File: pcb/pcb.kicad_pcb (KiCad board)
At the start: 2 copper layers, 50 x 60 mm, 66 parts, among them J1 Battery, J10 Conn_01x04_Male, J11 STM32_SWD, J2 MOTOR_Vcc, J3 MOTOR_5V, J4 MOTOR_OUT, J5 US_SENSOR, J6 BUMPER_SENSOR_FRONT, J7 BUMPER_SENSOR_BACK, J8 BT_USART, J9 GPIO, SW1 SW_Push, U1 LM317_TO-252, U2 L293D, U3 AMS1117-5.0, U4 AMS1117-3.3, U5 STM32F103C8T6, Y1 X322516MLB4SI

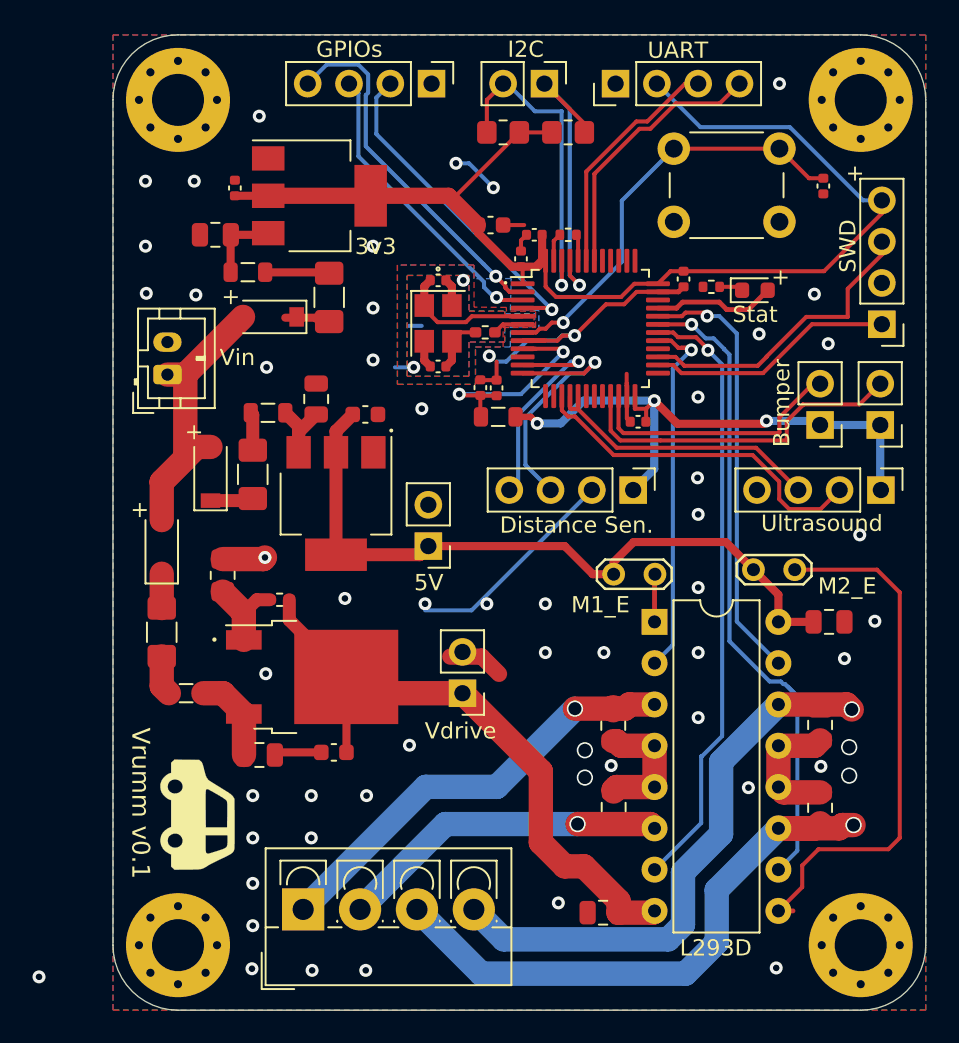
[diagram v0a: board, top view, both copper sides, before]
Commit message: SWD fix on pcb
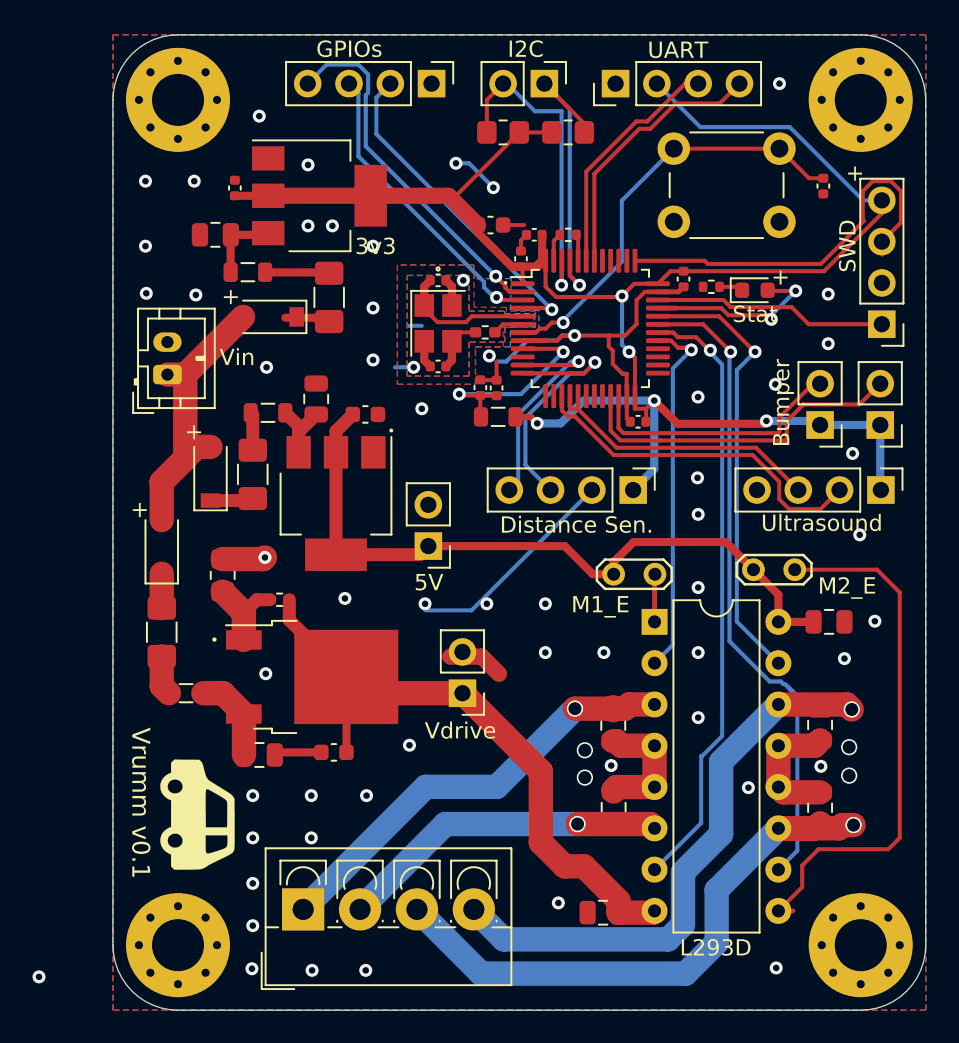
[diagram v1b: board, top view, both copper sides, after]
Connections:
- U5 pad 26: SYS_SWDIO -> Net-(U5-Pad26)
- U5 pad 27: SYS_SWCLK -> Net-(U5-Pad27)
- U5 pad 34: Net-(U5-Pad34) -> SYS_SWDIO
- U5 pad 37: Net-(U5-Pad37) -> SYS_SWCLK
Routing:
- net +3V3: track 114.5 -> 121.0 mm, vias 3 -> 5
- net SYS_SWCLK: track 18.7 -> 24.4 mm
- net GND: track 74.1 -> 77.9 mm, vias 58 -> 62
- net Net-(D4-Pad2): track 7.59 -> 11.4 mm, vias 0 -> 2
- net SYS_SWDIO: track 15.2 -> 14.4 mm
- net MOTOR2_CH2: track 26.8 -> 27.6 mm

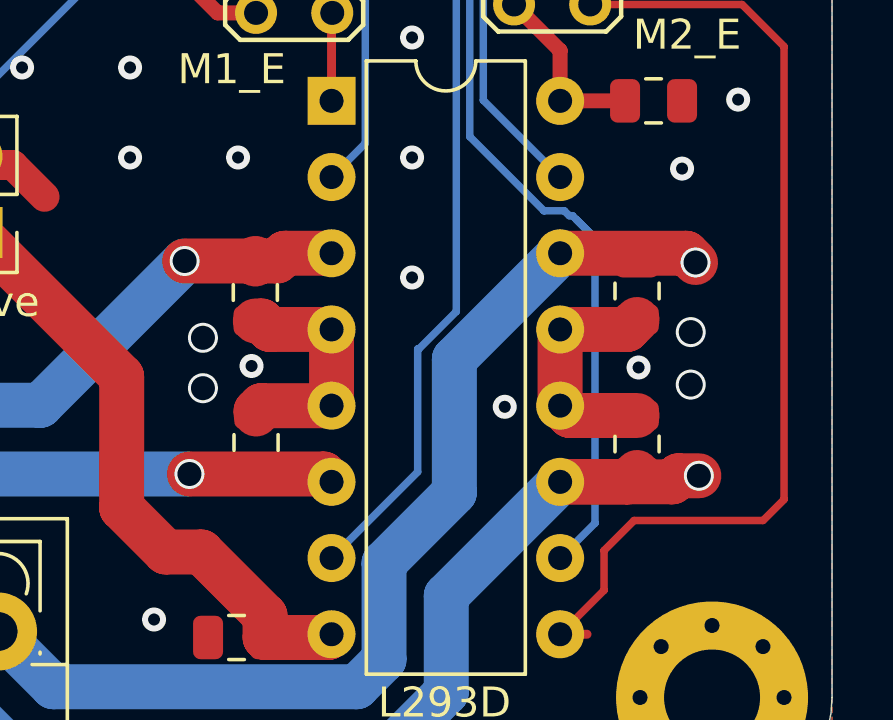
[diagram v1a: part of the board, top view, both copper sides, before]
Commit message: PCB: voltage divider on motor power
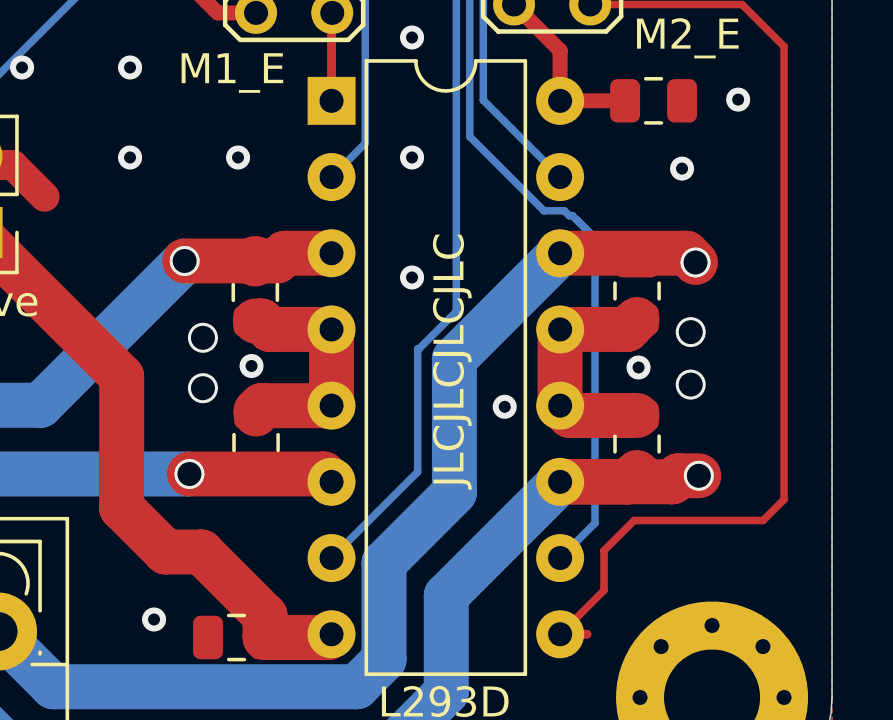
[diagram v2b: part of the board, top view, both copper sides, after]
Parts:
- R1: value 5.6k -> 1.5k
- R2: value 1k -> 240
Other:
- board text added: "+9.1V"
- board text added: "JLCJLCJLCJLC"
- board text added: "VCC"
- board text removed: "+8.5V"
- board text removed: "Vcc"
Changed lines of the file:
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@@
   (general
     (thickness 1.6)
-    (drawings 65)
+    (drawings 66)
     (tracks 531)
     (zones 0)
@@
       (effects (font (size 1 1) (thickness 0.15)))
     )
-    (fp_text value 1k (at 0 1.17) (layer F.Fab)
+    (fp_text value 240 (at 0 1.17) (layer F.Fab)
       (effects (font (size 1 1) (thickness 0.15)))
     )
@@
       (effects (font (size 1 1) (thickness 0.15)))
     )
-    (fp_text value 5.6k (at 0 1.65 90) (layer F.Fab)
+    (fp_text value 1.5k (at 0 1.65 90) (layer F.Fab)
       (effects (font (size 1 1) (thickness 0.15)))
     )
@@
     )
   )
+  (gr_text JLCJLCJLCJLC (at 49.25 56.75 90) (layer F.SilkS)
+    (effects (font (size 1 1) (thickness 0.15)))
+  )
   (gr_text + (at 57.65 20.5) (layer F.SilkS)
     (effects (font (size 1 1) (thickness 0.15)))
@@
     (effects (font (size 1 1) (thickness 0.15)) (justify mirror))
   )
-  (gr_text +8.5V (at 29.84 52.41) (layer B.SilkS)
+  (gr_text +9.1V (at 29.84 52.41) (layer B.SilkS)
     (effects (font (size 1 1) (thickness 0.15)) (justify mirror))
   )
@@
     (effects (font (size 1 1) (thickness 0.15)) (justify mirror))
   )
-  (gr_text Vcc (at 18.3 32.8) (layer B.SilkS)
+  (gr_text VCC (at 18.5 34) (layer B.SilkS)
     (effects (font (size 1 1) (thickness 0.15)) (justify mirror))
   )

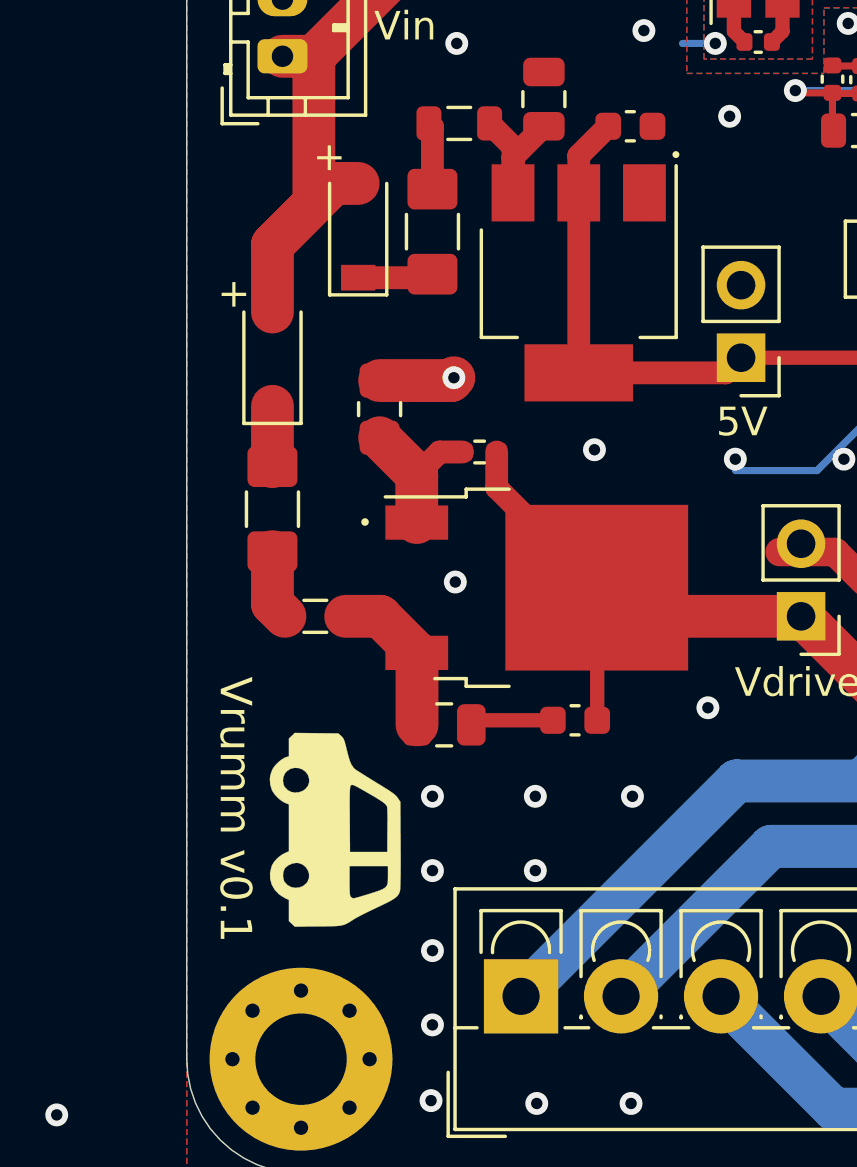
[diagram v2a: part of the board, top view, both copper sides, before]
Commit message: pcb versioning on silk layer, 5v track width
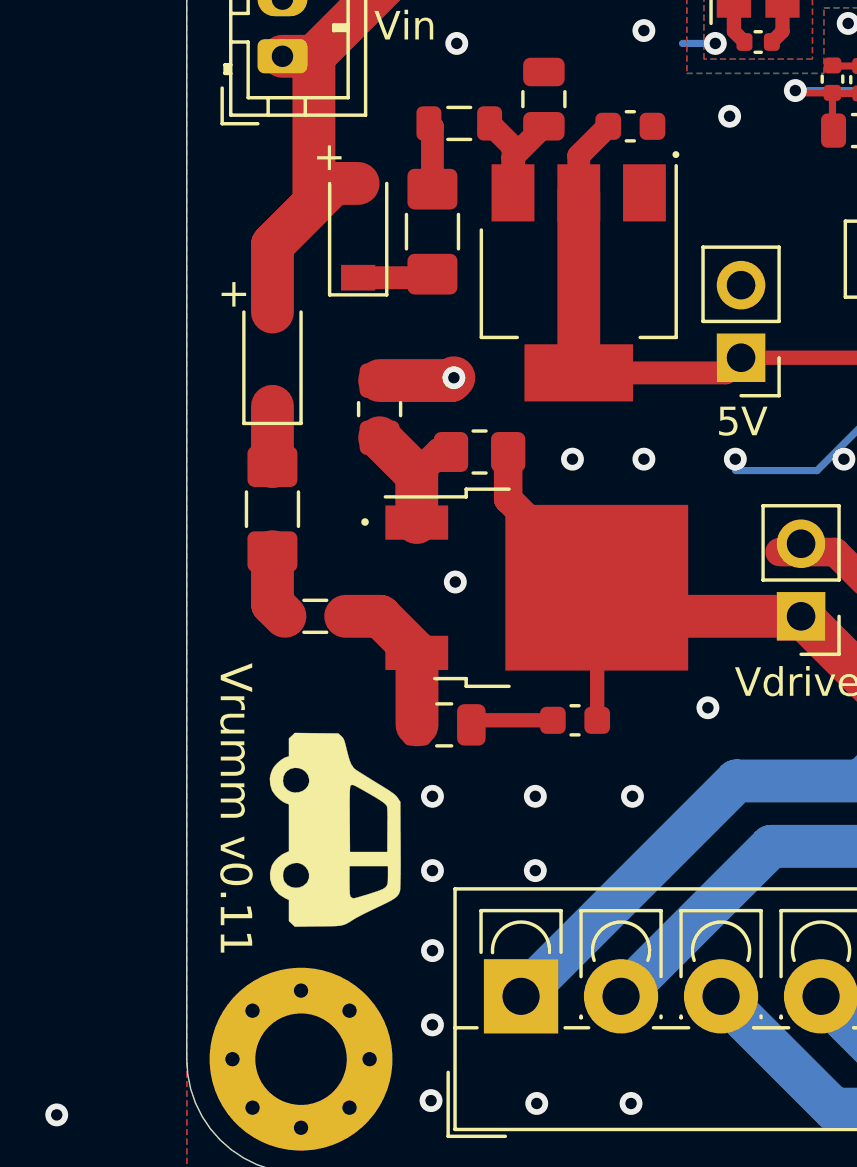
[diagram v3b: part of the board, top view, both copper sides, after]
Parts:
- R2: footprint Resistor_SMD:R_0402_1005Metric_Pad0.72x0.64mm_HandSolder -> Resistor_SMD:R_0805_2012Metric_Pad1.20x1.40mm_HandSolder
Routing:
- net GND: vias 62 -> 63
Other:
- board text added: "Vrumm v0.11"
- board text removed: "Vrumm v0.1"
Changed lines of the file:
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@@
     (thickness 1.6)
     (drawings 66)
-    (tracks 531)
+    (tracks 532)
     (zones 0)
     (modules 66)
@@
   )
   (setup
-    (last_trace_width 0.25)
+    (last_trace_width 1.5)
     (user_trace_width 0.3)
     (user_trace_width 0.4)
@@
     (add_net WHEEL_SENSOR_R)
   )
+  (module Resistor_SMD:R_0805_2012Metric_Pad1.20x1.40mm_HandSolder (layer F.Cu)
+    (at 22.25 46.75 180)
+    (descr "Resistor SMD 0805 (2012 Metric), square (rectangular) end terminal, IPC_7351 nominal with elongated pad for handsoldering. (Body size source: IPC-SM-782 page 72, https://www.pcb-3d.com/wordpress/wp-content/uploads/ipc-sm-782a_amendment_1_and_2.pdf), generated with kicad-footprint-generator")
+    (tags "resistor handsolder")
+    (attr smd)
+    (fp_text reference R2 (at 0 -1.65) (layer F.Fab)
+      (effects (font (size 1 1) (thickness 0.15)))
+    )
+    (fp_text value 240 (at 0 1.65) (layer F.Fab)
+      (effects (font (size 1 1) (thickness 0.15)))
+    )
+    (fp_text user %R (at 0 0) (layer F.Fab)
+      (effects (font (size 0.5 0.5) (thickness 0.08)))
+    )
+    (fp_line (start -1 0.625) (end -1 -0.625) (layer F.Fab) (width 0.1))
+    (fp_line (start -1 -0.625) (end 1 -0.625) (layer F.Fab) (width 0.1))
+    (fp_line (start 1 -0.625) (end 1 0.625) (layer F.Fab) (width 0.1))
+    (fp_line (start 1 0.625) (end -1 0.625) (layer F.Fab) (width 0.1))
+    (fp_line (start -0.227064 -0.735) (end 0.227064 -0.735) (layer F.SilkS) (width 0.12))
+    (fp_line (start -0.227064 0.735) (end 0.227064 0.735) (layer F.SilkS) (width 0.12))
+    (fp_line (start -1.85 0.95) (end -1.85 -0.95) (layer F.CrtYd) (width 0.05))
+    (fp_line (start -1.85 -0.95) (end 1.85 -0.95) (layer F.CrtYd) (width 0.05))
+    (fp_line (start 1.85 -0.95) (end 1.85 0.95) (layer F.CrtYd) (width 0.05))
+    (fp_line (start 1.85 0.95) (end -1.85 0.95) (layer F.CrtYd) (width 0.05))
+    (pad 2 smd roundrect (at 1 0 180) (size 1.2 1.4) (layers F.Cu F.Paste F.Mask) (roundrect_rratio 0.2083325)
+      (net 60 "Net-(R1-Pad2)"))
+    (pad 1 smd roundrect (at -1 0 180) (size 1.2 1.4) (layers F.Cu F.Paste F.Mask) (roundrect_rratio 0.2083325)
+      (net 44 Vdrive))
+    (model ${KISYS3DMOD}/Resistor_SMD.3dshapes/R_0805_2012Metric.wrl
+      (at (xyz 0 0 0))
+      (scale (xyz 1 1 1))
+      (rotate (xyz 0 0 0))
+    )
+  )
   (module Crystal:Crystal_SMD_3225-4Pin_3.2x2.5mm (layer F.Cu)
     (at 32 29.75 270)
@@
   (module logo_car:logo_car (layer F.Cu)
     (at 17.28 60 270)
+    (attr smd)
     (fp_text reference G*** (at 0 0 90) (layer F.SilkS) hide
       (effects (font (size 1.524 1.524) (thickness 0.3)))
@@
     )
   )
-  (module Resistor_SMD:R_0402_1005Metric_Pad0.72x0.64mm_HandSolder (layer F.Cu)
-    (at 22.25 46.75 180)
-    (descr "Resistor SMD 0402 (1005 Metric), square (rectangular) end terminal, IPC_7351 nominal with elongated pad for handsoldering. (Body size source: IPC-SM-782 page 72, https://www.pcb-3d.com/wordpress/wp-content/uploads/ipc-sm-782a_amendment_1_and_2.pdf), generated with kicad-footprint-generator")
-    (tags "resistor handsolder")
-    (attr smd)
-    (fp_text reference R2 (at -58.5 -4) (layer F.Fab)
-      (effects (font (size 1 1) (thickness 0.15)))
-    )
-    (fp_text value 240 (at 0 1.17) (layer F.Fab)
-      (effects (font (size 1 1) (thickness 0.15)))
-    )
-    (fp_line (start 1.1 0.47) (end -1.1 0.47) (layer F.CrtYd) (width 0.05))
-    (fp_line (start 1.1 -0.47) (end 1.1 0.47) (layer F.CrtYd) (width 0.05))
-    (fp_line (start -1.1 -0.47) (end 1.1 -0.47) (layer F.CrtYd) (width 0.05))
-    (fp_line (start -1.1 0.47) (end -1.1 -0.47) (layer F.CrtYd) (width 0.05))
-    (fp_line (start -0.167621 0.38) (end 0.167621 0.38) (layer F.SilkS) (width 0.12))
-    (fp_line (start -0.167621 -0.38) (end 0.167621 -0.38) (layer F.SilkS) (width 0.12))
-    (fp_line (start 0.525 0.27) (end -0.525 0.27) (layer F.Fab) (width 0.1))
-    (fp_line (start 0.525 -0.27) (end 0.525 0.27) (layer F.Fab) (width 0.1))
-    (fp_line (start -0.525 -0.27) (end 0.525 -0.27) (layer F.Fab) (width 0.1))
-    (fp_line (start -0.525 0.27) (end -0.525 -0.27) (layer F.Fab) (width 0.1))
-    (fp_text user %R (at 0 0) (layer F.Fab)
-      (effects (font (size 0.26 0.26) (thickness 0.04)))
-    )
-    (pad 2 smd roundrect (at 0.5975 0 180) (size 0.715 0.64) (layers F.Cu F.Paste F.Mask) (roundrect_rratio 0.25)
-      (net 60 "Net-(R1-Pad2)"))
-    (pad 1 smd roundrect (at -0.5975 0 180) (size 0.715 0.64) (layers F.Cu F.Paste F.Mask) (roundrect_rratio 0.25)
-      (net 44 Vdrive))
-    (model ${KISYS3DMOD}/Resistor_SMD.3dshapes/R_0402_1005Metric.wrl
-      (at (xyz 0 0 0))
-      (scale (xyz 1 1 1))
-      (rotate (xyz 0 0 0))
-    )
-  )
   (module Resistor_SMD:R_0805_2012Metric_Pad1.20x1.40mm_HandSolder (layer F.Cu)
     (at 18.75 45.25 270)
@@
     (effects (font (size 0.8 0.8) (thickness 0.15)) (justify mirror))
   )
-  (gr_text "Vrumm v0.1" (at 13.7 59.27 270) (layer F.SilkS)
+  (gr_text "Vrumm v0.11" (at 13.7 59.27 270) (layer F.SilkS)
     (effects (font (size 1.1 1.1) (thickness 0.2)))
   )
@@
   (segment (start 16.45 38.05) (end 15 39.5) (width 1.5) (layer F.Cu) (net 1))
   (segment (start 16.45 32.9) (end 16.45 38.05) (width 1.5) (layer F.Cu) (net 1))
-  (via (at 26.27 46.67) (size 0.8) (drill 0.4) (layers F.Cu B.Cu) (net 2))
+  (via (at 25.5 47) (size 0.8) (drill 0.4) (layers F.Cu B.Cu) (net 2))
   (via (at 40.4 30.5) (size 0.8) (drill 0.4) (layers F.Cu B.Cu) (net 2))
   (via (at 30.5 32.45) (size 0.8) (drill 0.4) (layers F.Cu B.Cu) (net 2))
@@
   (via (at 25.5 23.75) (size 0.8) (drill 0.4) (layers F.Cu B.Cu) (net 2))
   (via (at 24 20) (size 0.8) (drill 0.4) (layers F.Cu B.Cu) (net 2))
+  (via (at 28 47) (size 0.8) (drill 0.4) (layers F.Cu B.Cu) (net 2))
   (via (at 43.75 31.5) (size 0.8) (drill 0.4) (layers F.Cu B.Cu) (net 11))
   (via (at 52.5 29.5) (size 0.8) (drill 0.4) (layers F.Cu B.Cu) (net 18))
   (segment (start 25.72 36.38) (end 26.75 35.35) (width 0.8) (layer F.Cu) (net 3))
   (segment (start 25.72 37.68) (end 25.72 36.38) (width 0.8) (layer F.Cu) (net 3))
-  (segment (start 25.72 37.68) (end 25.72 43.98) (width 0.8) (layer F.Cu) (net 3))
   (segment (start 30.87 43.98) (end 31.4 43.45) (width 0.8) (layer F.Cu) (net 3))
   (segment (start 25.72 43.98) (end 30.87 43.98) (width 0.8) (layer F.Cu) (net 3))
@@
   (segment (start 41.52 45.18) (end 42.8 45.18) (width 0.5) (layer F.Cu) (net 3))
   (segment (start 39.79 43.45) (end 41.52 45.18) (width 0.5) (layer F.Cu) (net 3))
+  (segment (start 25.72 37.68) (end 25.72 43.98) (width 1.5) (layer F.Cu) (net 3))
   (segment (start 23.78 36.07) (end 23.42 36.07) (width 0.4) (layer F.Cu) (net 4))
   (segment (start 24.5 35.35) (end 23.78 36.07) (width 0.4) (layer F.Cu) (net 4))
@@
   (segment (start 38.32 57.3) (end 38.32 61.68) (width 1.5) (layer F.Cu) (net 44))
   (segment (start 33.52 52.5) (end 38.32 57.3) (width 1.5) (layer F.Cu) (net 44))
-  (segment (start 22.8475 47.9975) (end 26.35 51.5) (width 0.8) (layer F.Cu) (net 44))
-  (segment (start 22.8475 46.75) (end 22.8475 47.9975) (width 0.8) (layer F.Cu) (net 44))
+  (segment (start 23.25 48.4) (end 26.35 51.5) (width 1) (layer F.Cu) (net 44))
+  (segment (start 23.25 46.75) (end 23.25 48.4) (width 1) (layer F.Cu) (net 44))
   (segment (start 18.77 52.5) (end 20.05 53.78) (width 1.5) (layer F.Cu) (net 57))
   (segment (start 17.5625 52.5) (end 18.77 52.5) (width 1.5) (layer F.Cu) (net 57))
@@
   (segment (start 18.75 46.25) (end 20.05 47.55) (width 1.5) (layer F.Cu) (net 60))
   (segment (start 20.05 47.55) (end 20.05 49.22) (width 1.5) (layer F.Cu) (net 60))
-  (segment (start 20.85 46.75) (end 20.05 47.55) (width 0.8) (layer F.Cu) (net 60))
-  (segment (start 21.6525 46.75) (end 20.85 46.75) (width 0.8) (layer F.Cu) (net 60))
+  (segment (start 20.85 46.75) (end 20.05 47.55) (width 1) (layer F.Cu) (net 60))
+  (segment (start 21.25 46.75) (end 20.85 46.75) (width 1) (layer F.Cu) (net 60))
   (zone (net 2) (net_name GND) (layer F.Cu) (hatch edge 0.508)
     (connect_pads (clearance 0.508))
